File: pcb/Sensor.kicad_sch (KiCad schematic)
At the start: 0 parts

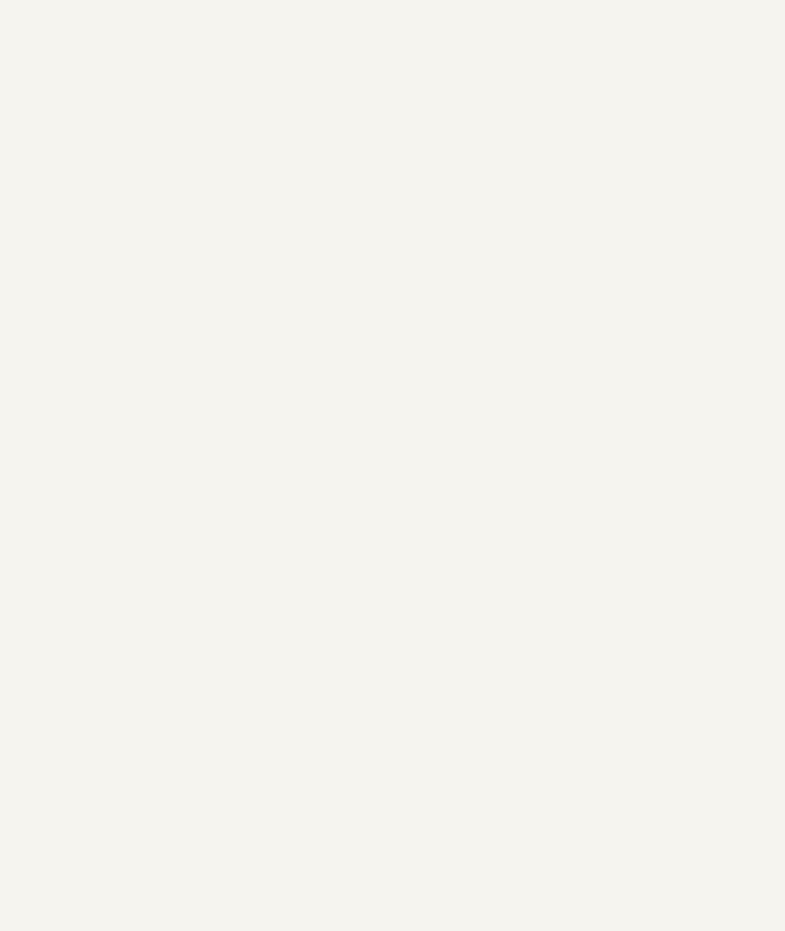
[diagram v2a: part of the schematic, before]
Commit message: added spark detection
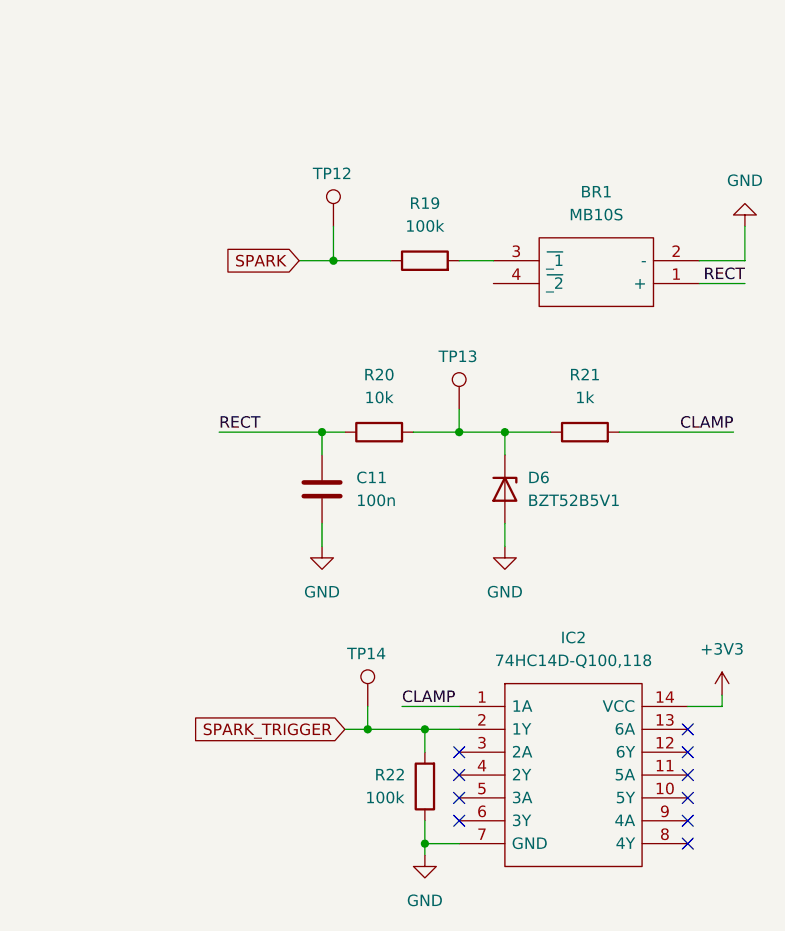
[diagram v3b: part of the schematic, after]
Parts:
- added BR1: MB10S, SOP245P670X290-4N, symbol SamacSys_Parts:MB10S
- added C11: 100n, Capacitor_THT:C_Disc_D4.3mm_W1.9mm_P5.00mm, symbol Device:C
- added D6: BZT52B5V1, symbol Device:D_Zener
- added IC2: 74HC14D-Q100,118, SOIC127P600X175-14N, symbol SamacSys_Parts:74HC14D-Q100,118
- added R19: 100k, Resistor_THT:R_Axial_DIN0204_L3.6mm_D1.6mm_P1.90mm_Vertical, symbol Device:R
- added R20: 10k, Resistor_THT:R_Axial_DIN0204_L3.6mm_D1.6mm_P1.90mm_Vertical, symbol Device:R
- added R21: 1k, Resistor_SMD:R_0201_0603Metric, symbol Device:R
- added R22: 100k, Resistor_SMD:R_0201_0603Metric, symbol Device:R
- added TP12, TP13, TP14: TestPoint, symbol Connector:TestPoint
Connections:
- new net: D6.1 (K), R20.2, R21.1, TP13.1
- new net: BR1.3 (~{_1}), R19.2
- new net +3V3: IC2.14 (VCC)
- new net CLAMP: IC2.1 (1A), R21.2
- new net GND: BR1.2 (-), C11.2, D6.2 (A), IC2.7 (GND), R22.1
- new net RECT: BR1.1 (+), C11.1, R20.1
- new net SPARK: R19.1, TP12.1
- new net SPARK_TRIGGER: IC2.2 (1Y), R22.2, TP14.1
- no-connect marks 0 -> 10

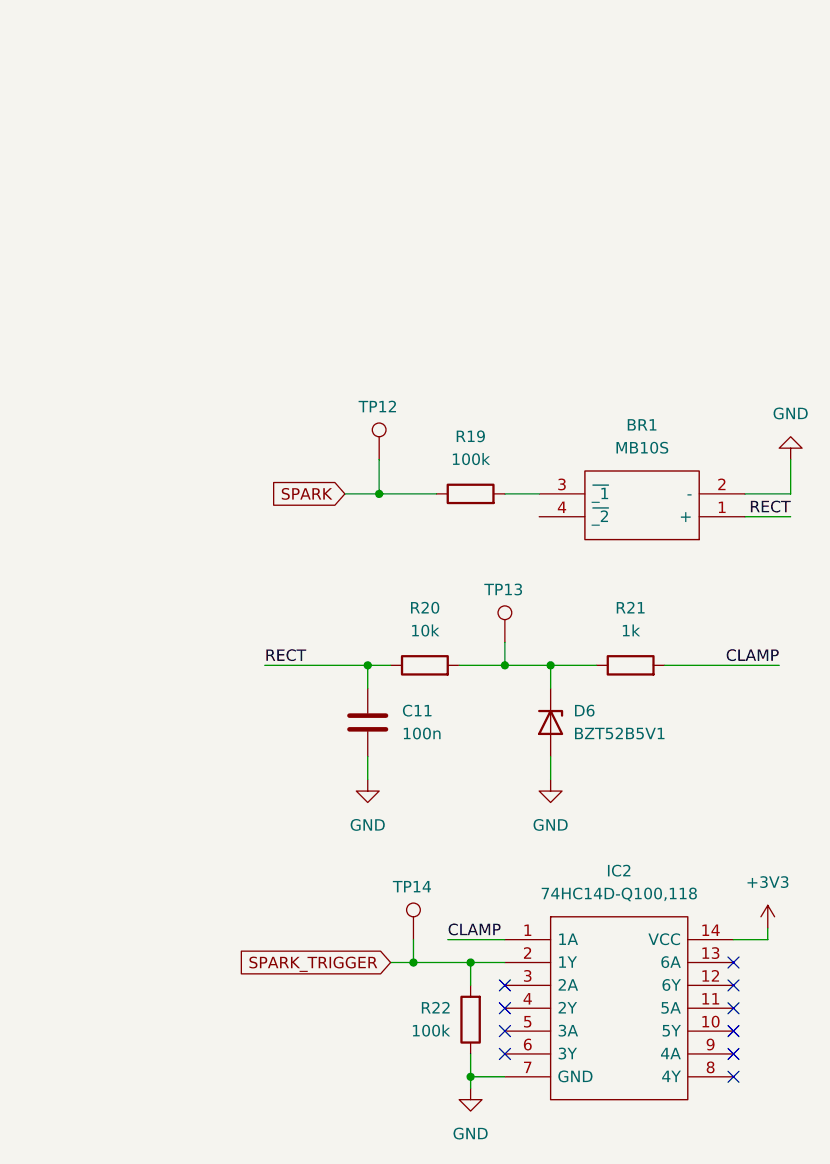
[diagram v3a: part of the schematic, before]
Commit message: added batteryless function
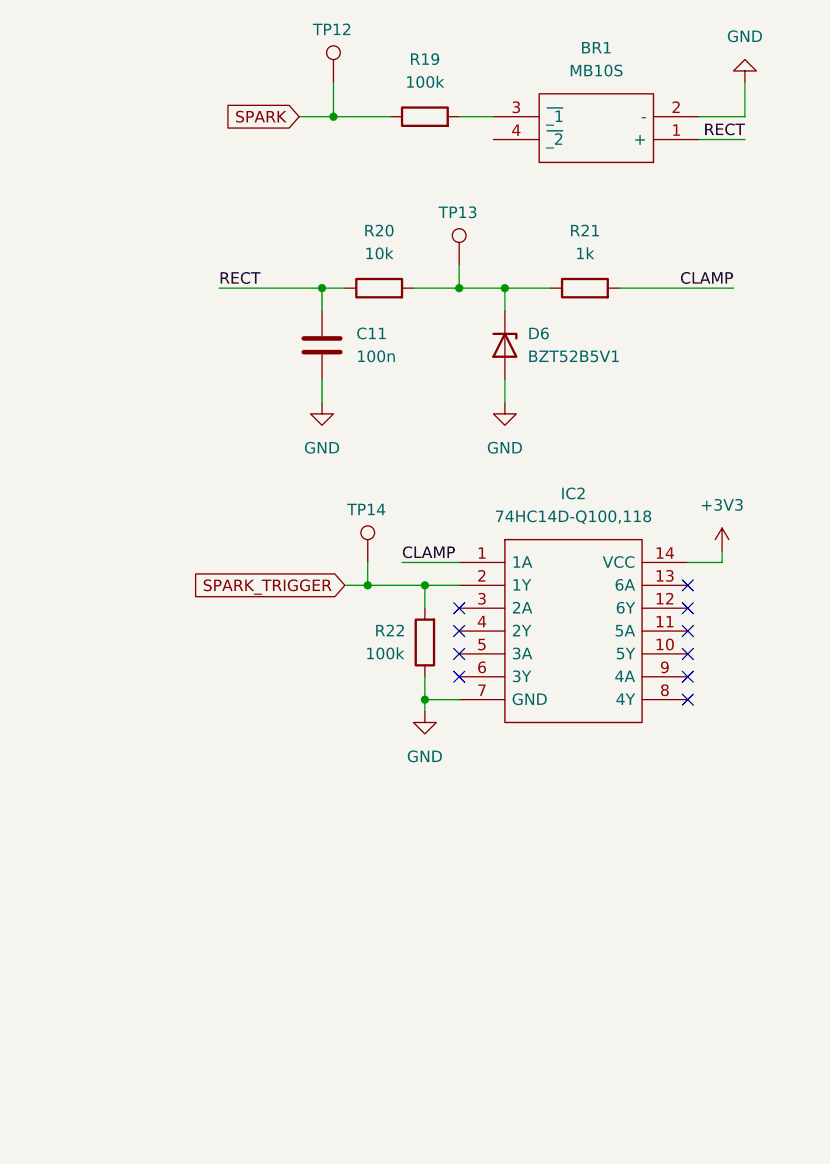
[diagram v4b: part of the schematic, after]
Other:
- moved on the sheet: BR1, C11, D6, IC2, R19, R20, R21, R22, TP12, TP13, TP14

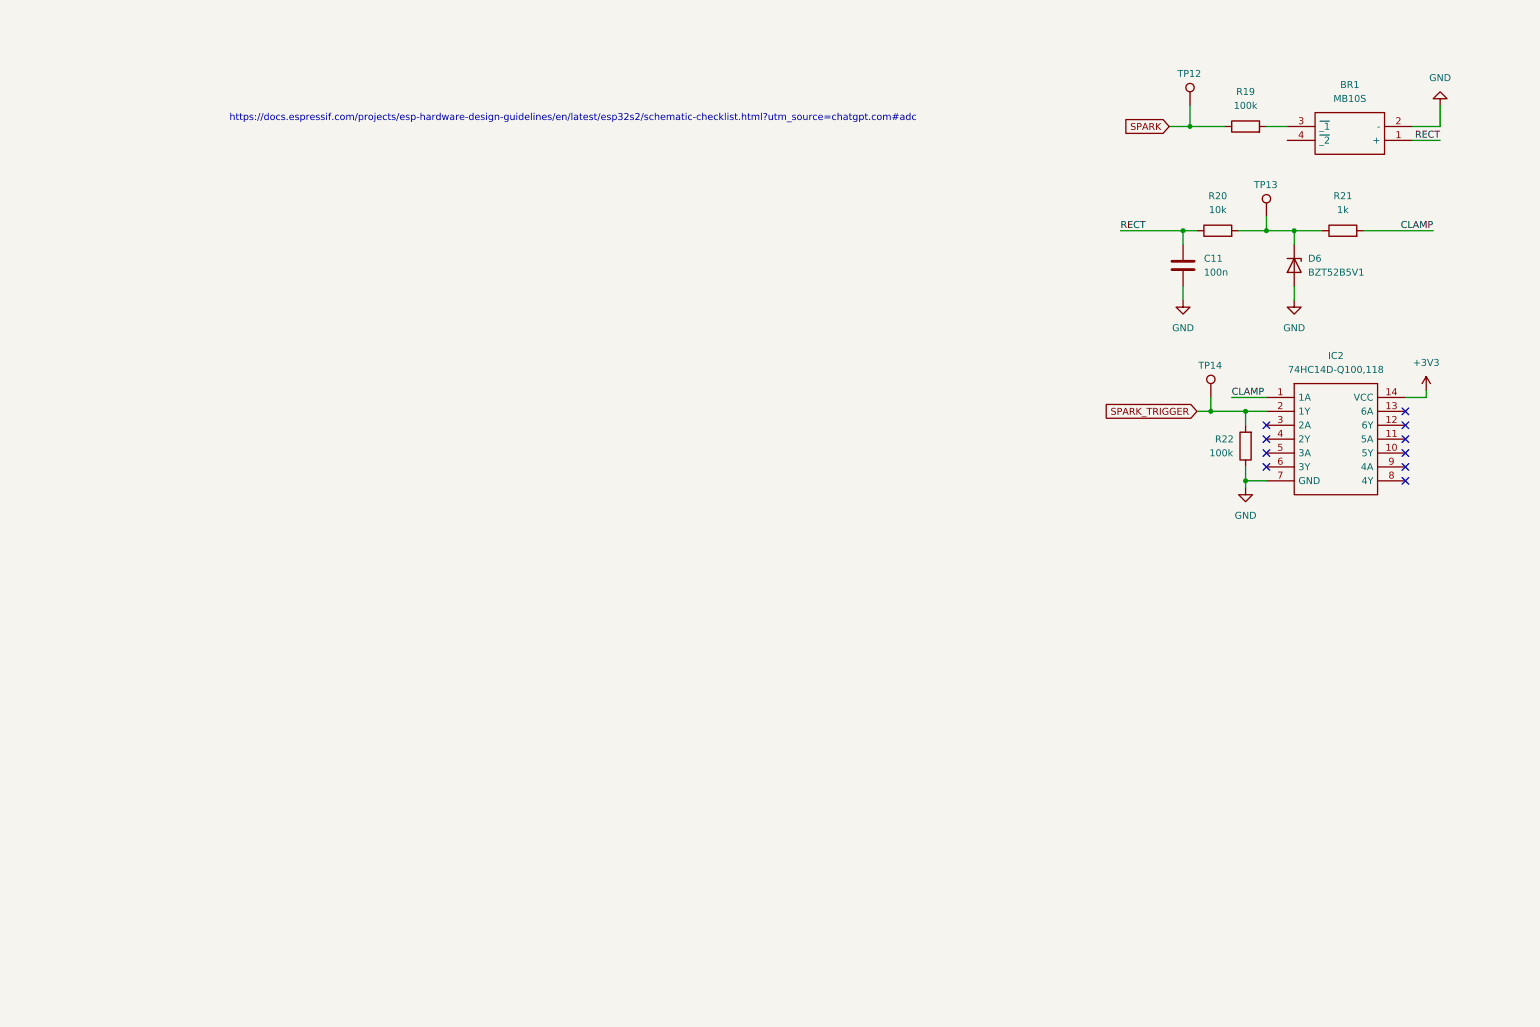
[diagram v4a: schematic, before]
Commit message: added predisposition for second piezo conditioning circuit
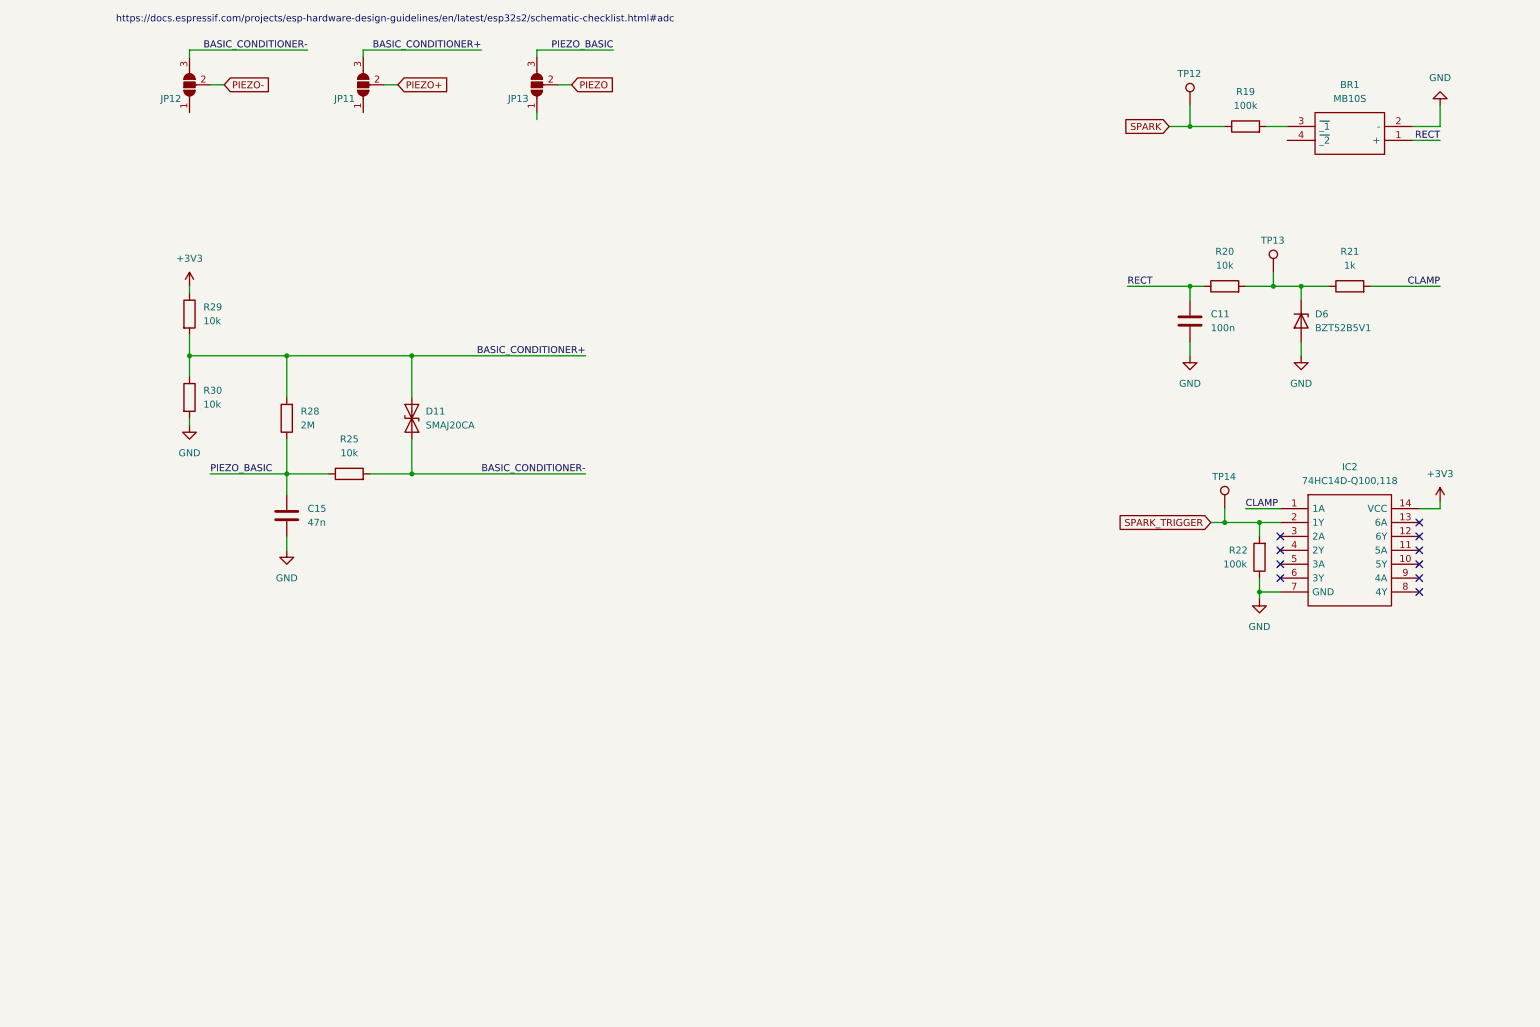
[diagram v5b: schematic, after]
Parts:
- added C15: 47n, Capacitor_THT:C_Disc_D4.3mm_W1.9mm_P5.00mm, symbol Device:C
- added D11: SMAJ20CA, Diode_SMD:D_SMA, symbol Diode:SMAJ20CA
- added JP11, JP12, JP13: SolderJumper_3_Open, Jumper:SolderJumper-3_P1.3mm_Open_RoundedPad1.0x1.5mm, symbol Jumper:SolderJumper_3_Open
- added R25: 10k, Resistor_THT:R_Axial_DIN0204_L3.6mm_D1.6mm_P1.90mm_Vertical, symbol Device:R
- added R28: 2M, Resistor_THT:R_Axial_DIN0204_L3.6mm_D1.6mm_P1.90mm_Vertical, symbol Device:R
- added R29, R30: 10k, Resistor_SMD:R_0201_0603Metric, symbol Device:R
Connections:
- net +3V3: now also R29.1
- net GND: now also C15.2, R30.2
- new net BASIC_CONDITIONER+: D11.2 (A2), JP11.3 (B), R28.2, R29.2, R30.1
- new net BASIC_CONDITIONER-: D11.1 (A1), JP12.3 (B), R25.2
- new net PIEZO: JP13.2 (C)
- new net PIEZO+: JP11.2 (C)
- new net PIEZO-: JP12.2 (C)
- new net PIEZO_BASIC: C15.1, JP13.3 (B), R25.1, R28.1
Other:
- note added: "https://docs.espressif.com/projects/esp-hardware-design-guidelines/en/latest/esp32s2/schematic-checklist.html#adc"
- note removed: "https://docs.espressif.com/projects/esp-hardware-design-guidelines/en/latest/esp32s2/schematic-checklist.html?utm_source=chatgpt.com#adc"
- moved on the sheet: C11, D6, IC2, R20, R21, R22, TP13, TP14

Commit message: video call revision
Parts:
- added C16, C18: 22n, Capacitor_THT:C_Disc_D4.3mm_W1.9mm_P5.00mm, symbol Device:C
- added JP14, JP15: SolderJumper_2_Open, Jumper:SolderJumper-2_P1.3mm_Open_RoundedPad1.0x1.5mm, symbol Jumper:SolderJumper_2_Open
- added R31, R32: 4M7, Resistor_THT:R_Axial_DIN0204_L3.6mm_D1.6mm_P1.90mm_Vertical, symbol Device:R
- added U2: OPA376xxD, Package_SO:SOIC-8_3.9x4.9mm_P1.27mm, symbol Amplifier_Operational:OPA376xxD
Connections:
- net GND: now also JP11.1 (A), U2.3 (+), U2.4 (V-)
- net CHARGE_AMP-: now reaches JP12.1 (A)
- net CHARGE_AMP-: now also C16.1, C18.1, R31.1, R32.1, U2.2 (-)
- net PIEZO_AMP: now reaches JP13.1 (A)
- net PIEZO_AMP: now also C16.2, JP14.1 (A), JP15.1 (A), R31.2, U2.6
- new net: C18.2, JP14.2 (B)
- new net: JP15.2 (B), R32.2
- new net +3.3V: U2.7 (V+)
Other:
- moved on the sheet: JP11, JP12, JP13
